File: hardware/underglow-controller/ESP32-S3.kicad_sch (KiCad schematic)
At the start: 47 parts, among them J6 CONSOLE, J7 U.FL-R-SMT-1(10), SW2 SW_Push, SW3 SW_Push, U4 ESP32-S3R2, U5 W25Q128JVS, Y2 40MHZ, Y3 32.7k

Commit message: i can't believe what they did to my boy
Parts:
- removed C19, C23: 10pF, Capacitor_SMD:C_0402_1005Metric, symbol Device:C_Small
- removed TP10: CS1, TestPoint:TestPoint_Pad_D1.0mm, symbol Connector:TestPoint
- removed TP11: CS2, TestPoint:TestPoint_Pad_D1.0mm, symbol Connector:TestPoint
- removed TP2: CHIP_PU, TestPoint:TestPoint_Pad_D1.0mm, symbol Connector:TestPoint
- removed TP5: MOSI, TestPoint:TestPoint_Pad_D1.0mm, symbol Connector:TestPoint
- removed TP6: MISO, TestPoint:TestPoint_Pad_D1.0mm, symbol Connector:TestPoint
- removed TP8: SCLK, TestPoint:TestPoint_Pad_D1.0mm, symbol Connector:TestPoint
- removed TP9: CS0, TestPoint:TestPoint_Pad_D1.0mm, symbol Connector:TestPoint
- removed Y3: 32.7k, Crystal:Crystal_SMD_MicroCrystal_CC7V-T1A-2Pin_3.2x1.5mm, symbol Device:Crystal_Small
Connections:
- net CAN_N: now also U4.24 (GPIO18); no longer U4.23 (GPIO17)
- net CAN_P: now also U4.23 (GPIO17); no longer U4.24 (GPIO18)
- net FSPICS1: now also U4.5 (GPIO0); no longer U4.14 (GPIO9)
- net FSPICS2: now also U4.38 (GPIO33); no longer U4.18 (GPIO13)
- net SX1276_IRQ: now also U4.7 (GPIO2); no longer U4.6 (GPIO1)
- net SX1276_RESET: now also U4.6 (GPIO1); no longer U4.7 (GPIO2)
- net VSENSE: now also U4.18 (GPIO13); no longer U4.43 (GPIO38)
- no-connect marks 8 -> 7
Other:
- note removed: "CX1 = CX2 = 2(7pF - 2pF) = 10pF"

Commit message: updates nearly complete
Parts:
- C10, C14, C4, C7, C8: MPN C0805C104M3RAC7800 -> 560L104YTT
- C12, C15, C16: MPN (none) -> GRT21BC81A106KE01L
- R16, R17, R22, R28: MPN (none) -> RC0402JR-070RP
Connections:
- net SPICS1 is gone; now on net MCPWM_FAULT: U4.28 (SPICS1)
- net GPIO45: now also U4.51 (GPIO45)
- net GPIO46: now also U4.52 (GPIO46)
- no-connect marks 7 -> 5
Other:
- moved on the sheet: C18, C22, Y2

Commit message: add USB VIN
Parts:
- renumbered AE2 to AE4, C10 to C38, C11 to C39, C12 to C40, C14 to C41, C16 to C42, C13 to C43, C15 to C44, C8 to C45, C7 to C46, C17 to C47, C20 to C48, C21 to C49, C4 to C50, C37 to C51, C18 to C52, C22 to C53, J6 to J4, J7 to J5, L3 to L10, L4 to L11, R4 to R13, R6 to R14, R16 to R15, R17 to R16, R22 to R17, R15 to R18, R28 to R19, R25 to R20, R26 to R21, R27 to R22, SW2 to SW4, SW3 to SW5, U4 to U5, U5 to U6, Y2 to Y4

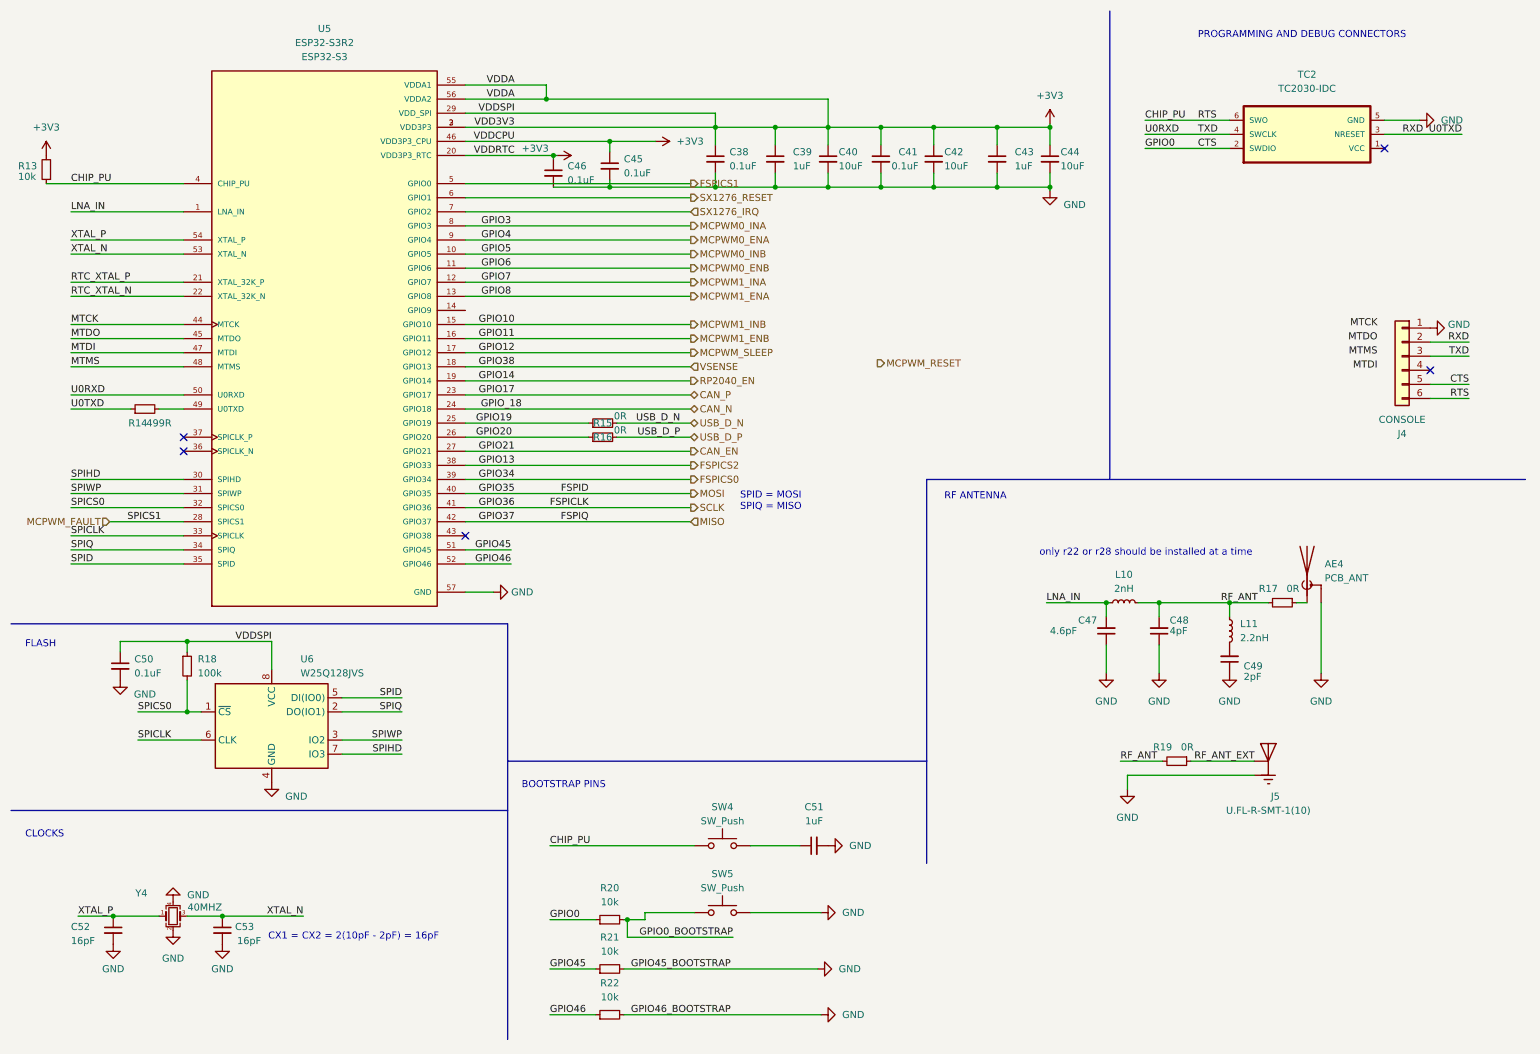
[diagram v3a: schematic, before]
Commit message: Hardware updates
* fix messed up +12v pin
* add a ground output for neopixels on both channels
* add a i2c microphone
* clean up schematic
* calculate component values for the LED drivers
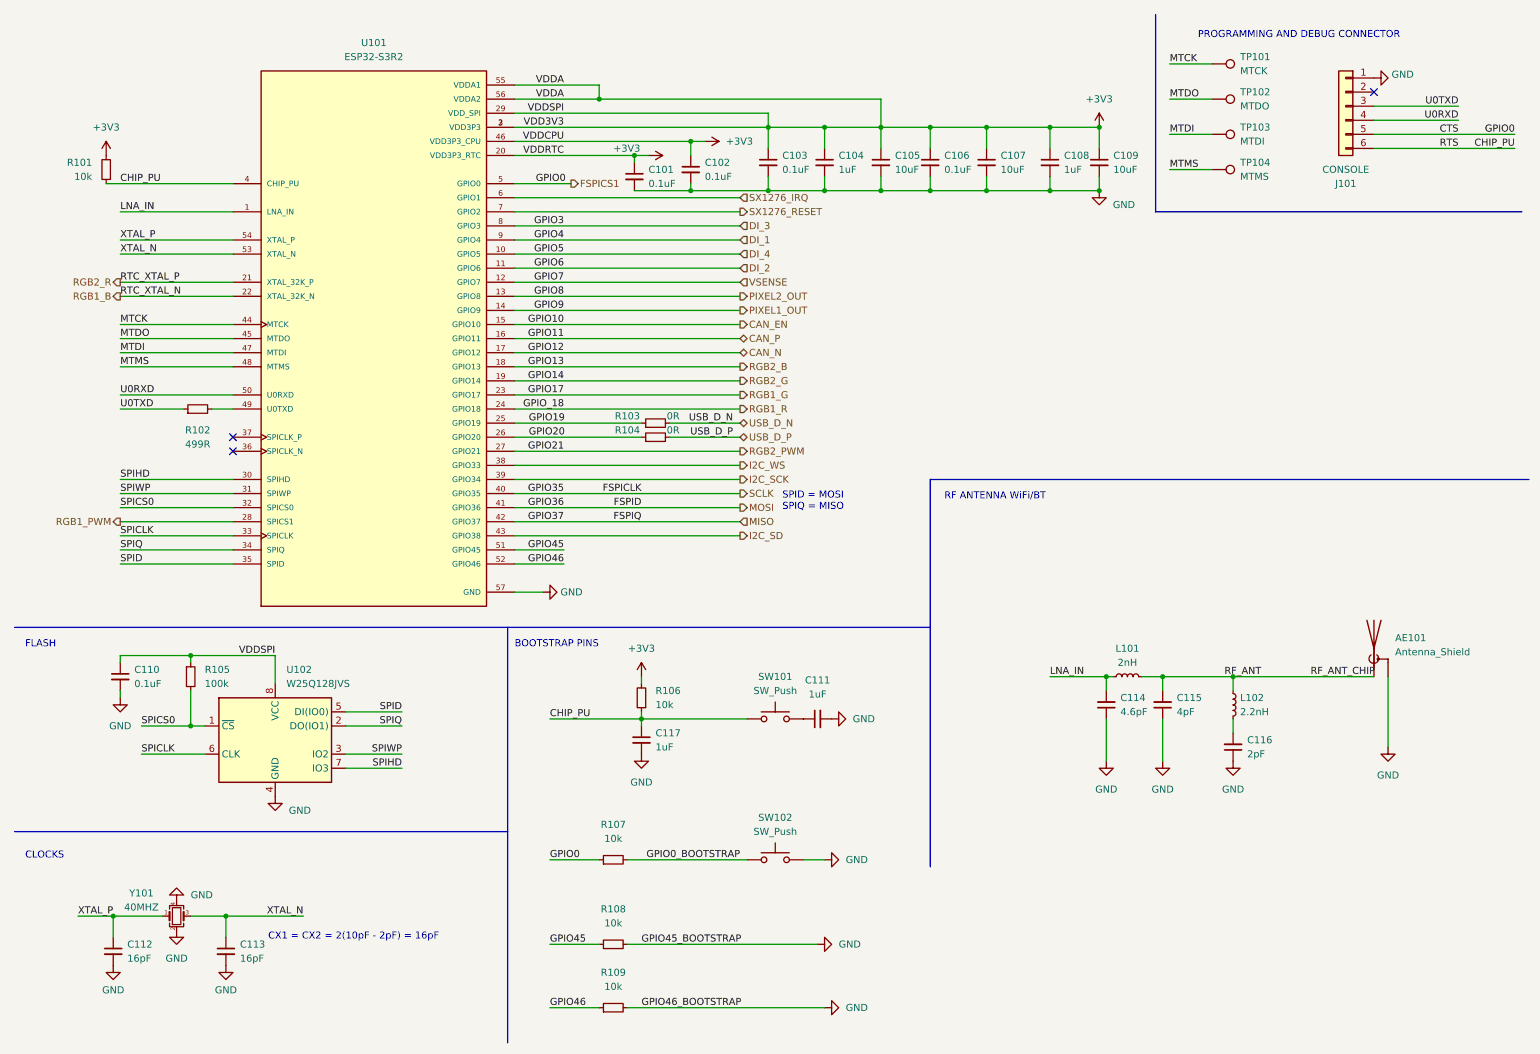
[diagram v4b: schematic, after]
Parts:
- removed AE4: PCB_ANT, RF_Antenna:Texas_SWRA117D_2.4GHz_Right, symbol Device:Antenna_Shield
- removed J5: U.FL-R-SMT-1(10), ConeCodes:HRS_U.FL-R-SMT-1(10), symbol U.FL-R-SMT-1_10_:U.FL-R-SMT-1(10)
- removed R17, R19: 0R, Resistor_SMD:R_0402_1005Metric, symbol Device:R_Small
- removed TC2: TC2030-IDC, Connector:Tag-Connect_TC2030-IDC-NL_2x03_P1.27mm_Vertical, symbol TDC-2030-IDC:TC2030-IDC
- added AE101: Antenna_Shield, RF_Antenna:Texas_SWRA117D_2.4GHz_Left, symbol Device:Antenna_Shield
- added C117: 1uF, Capacitor_SMD:C_0402_1005Metric, symbol Device:C_Small
- added R106: 10k, Resistor_SMD:R_0402_1005Metric, symbol Device:R_Small
- added TP101: MTCK, TestPoint:TestPoint_Pad_D1.0mm, symbol Connector:TestPoint
- added TP102: MTDO, TestPoint:TestPoint_Pad_D1.0mm, symbol Connector:TestPoint
- added TP103: MTDI, TestPoint:TestPoint_Pad_D1.0mm, symbol Connector:TestPoint
- added TP104: MTMS, TestPoint:TestPoint_Pad_D1.0mm, symbol Connector:TestPoint
- renumbered C46 to C101, C45 to C102, C38 to C103, C39 to C104, C40 to C105, C41 to C106, C42 to C107, C43 to C108, C44 to C109, C50 to C110, C51 to C111, C52 to C112, C53 to C113, C47 to C114, C48 to C115, C49 to C116, J4 to J101, L10 to L101, L11 to L102, R13 to R101, R14 to R102, R15 to R103, R16 to R104, R18 to R105, R20 to R107, R21 to R108, R22 to R109, SW4 to SW101, SW5 to SW102, U5 to U101, U6 to U102, Y4 to Y101
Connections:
- net CTS is gone; now on net FSPICS1: J101.5 (Pin_5), R107.1
- net MCPWM1_ENB is gone; now on net CAN_P: U101.16 (GPIO11)
- net MCPWM1_INA is gone; now on net VSENSE: U101.12 (GPIO7)
- net MCPWM1_INB is gone; now on net CAN_EN: U101.15 (GPIO10)
- net MCPWM_SLEEP is gone; now on net CAN_N: U101.17 (GPIO12)
- net +3V3: now also R106.2
- net CAN_EN: no longer U101.27 (GPIO21)
- net CAN_N: no longer U101.24 (GPIO18)
- net CAN_P: no longer U101.23 (GPIO17)
- net CHIP_PU: now also C117.1, R106.1
- net GND: now also AE101.2 (Shield), C117.2
- net MOSI: now also U101.41 (GPIO36); no longer U101.40 (GPIO35)
- net MTCK: now also TP101.1
- net MTDI: now also TP103.1
- net MTDO: now also TP102.1
- net MTMS: now also TP104.1
- net RF_ANT: now also AE101.1 (A)
- net SCLK: now also U101.40 (GPIO35); no longer U101.41 (GPIO36)
- net SX1276_IRQ: now also U101.6 (GPIO1); no longer U101.7 (GPIO2)
- net SX1276_RESET: now also U101.7 (GPIO2); no longer U101.6 (GPIO1)
- net VSENSE: no longer U101.18 (GPIO13)
- net U0RXD: now reaches J101.4 (Pin_4)
- net U0RXD: now also U101.50 (U0RXD)
- net PIXEL1_OUT: now reaches U101.14 (GPIO9)
- net I2C_SD: now reaches U101.43 (GPIO38)
- net FSPICS0 renamed I2C_SCK
- net FSPICS2 renamed I2C_WS
- net MCPWM0_ENA renamed DI_1
- net MCPWM0_ENB renamed DI_2
- net MCPWM0_INA renamed DI_3
- net MCPWM0_INB renamed DI_4
- net MCPWM1_ENA renamed PIXEL2_OUT
- net MCPWM_FAULT renamed RGB1_PWM
- net RP2040_EN renamed RGB2_G
- net RTC_XTAL_N renamed RGB1_B
- net RTC_XTAL_P renamed RGB2_R
- net RXD: no longer names the net of J101.2 (Pin_2)
- net RXD: no longer R102.1
- net TXD renamed U0TXD
- net U0TXD: now also R102.1; no longer U101.50 (U0RXD)
- new net RGB1_G: U101.23 (GPIO17)
- new net RGB1_R: U101.24 (GPIO18)
- new net RGB2_B: U101.18 (GPIO13)
- new net RGB2_PWM: U101.27 (GPIO21)
- no-connect marks 5 -> 3
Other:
- note added: "PROGRAMMING AND DEBUG CONNECTOR"
- note added: "RF ANTENNA WiFi/BT"
- note removed: "PROGRAMMING AND DEBUG CONNECTORS"
- note removed: "RF ANTENNA"
- note removed: "only r22 or r28 should be installed at a time"
- title: CAN RGB Controller -> CAN RGB Controller V5
- moved on the sheet: C101, C102, C103, C104, C105, C106, C107, C108, C109, C110, C111, C112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

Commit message: Bom fillout + wiring
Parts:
- C117: MPN (none) -> CGA2B1X7T0G105M050BC
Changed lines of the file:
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@@
       (effects (font (size 1.27 1.27)) hide)
     )
-    (property "Description" "" (id 4) (at 125.73 143.51 0)
+    (property "Description" "CAP CER 1UF 4V X7T 0402" (id 4) (at 125.73 143.51 0)
       (effects (font (size 1.27 1.27)) hide)
     )
-    (property "MPN" "" (id 5) (at 125.73 143.51 0)
+    (property "MPN" "CGA2B1X7T0G105M050BC" (id 5) (at 125.73 143.51 0)
       (effects (font (size 1.27 1.27)) hide)
     )

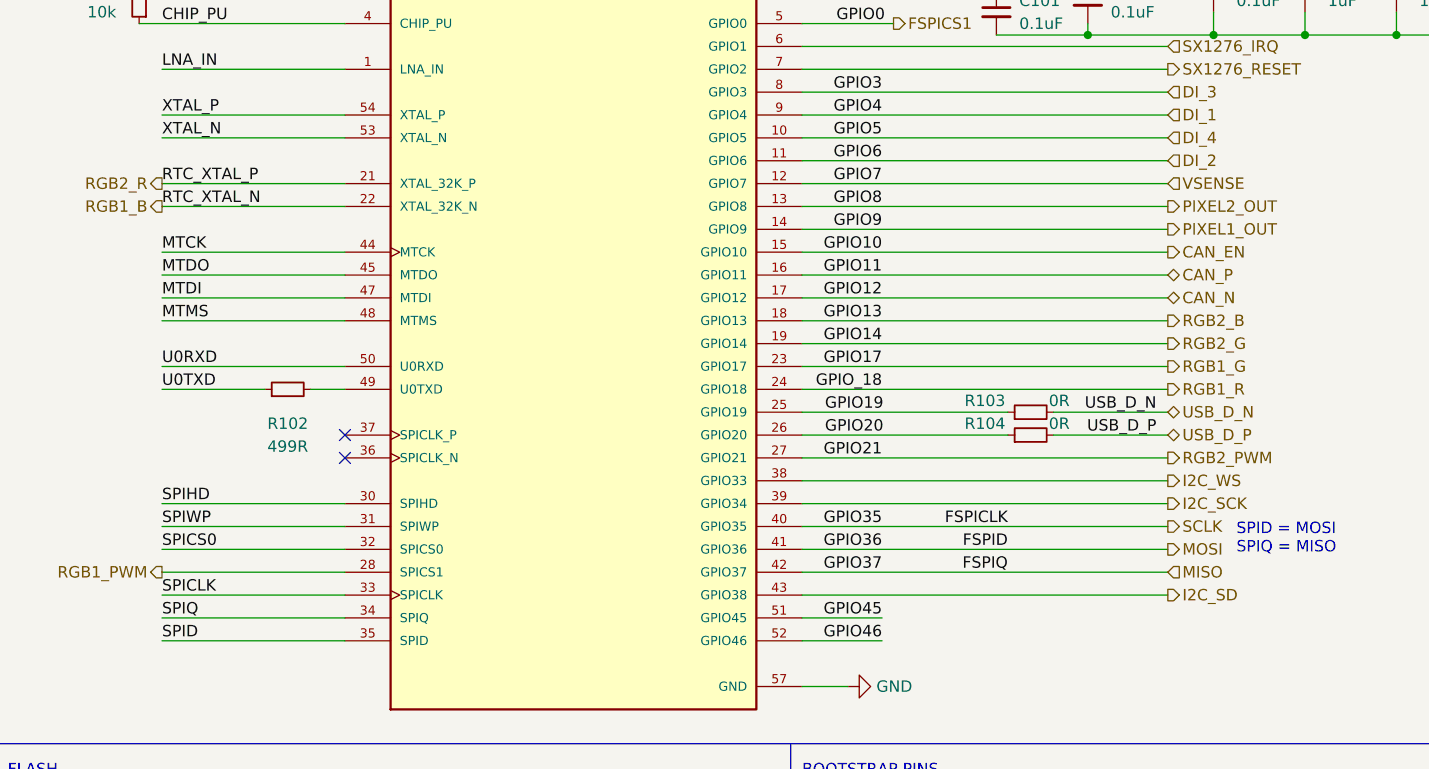
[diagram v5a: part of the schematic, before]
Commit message: hw updates based on prototype issues
* Removes unused hardware and firmware projectes
* Adds some documentation and bom
* cleanup READMEs
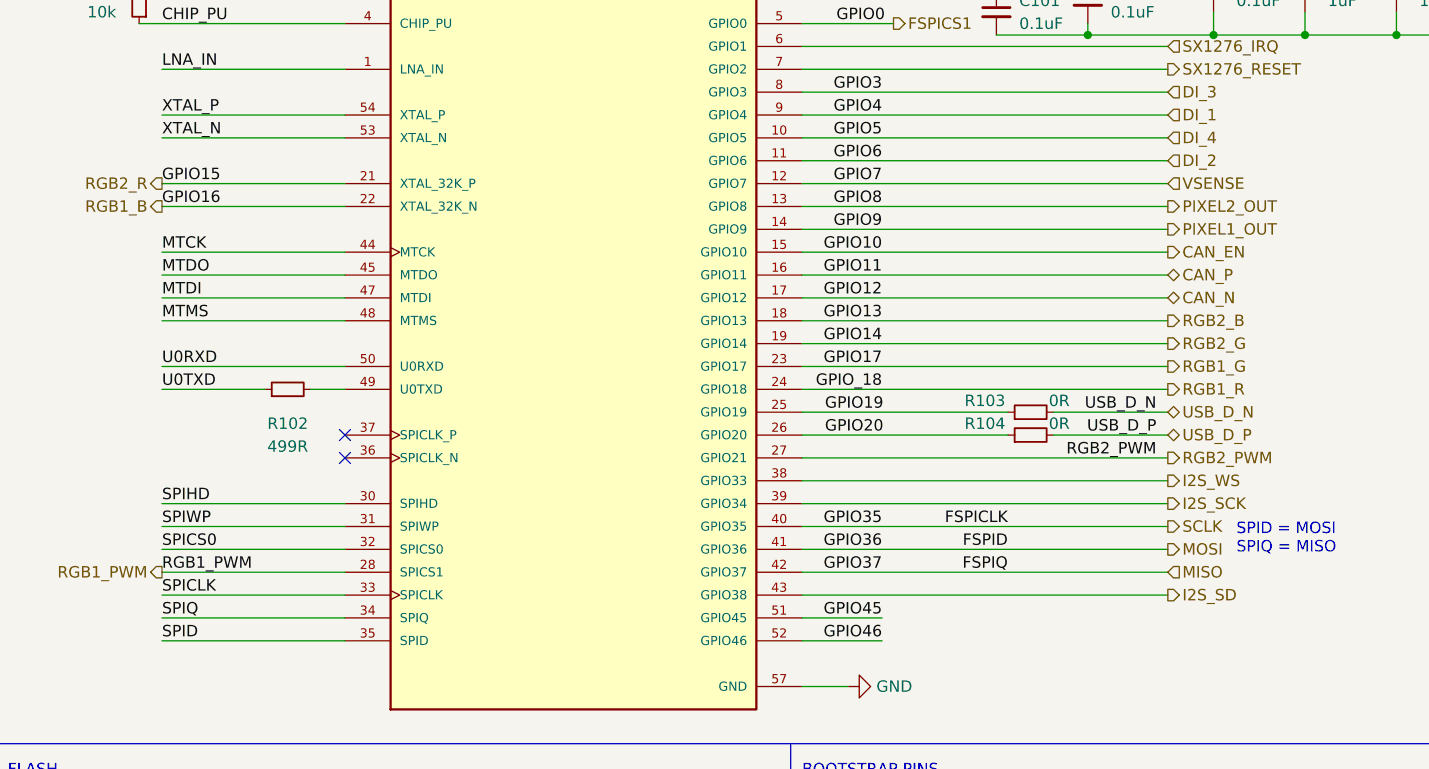
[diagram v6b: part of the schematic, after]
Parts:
- C101, C102, C103, C106, C110: MPN 560L104YTT -> CGA2B1X7R1C104M050BC
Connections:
- net I2C_SCK renamed I2S_SCK
- net I2C_SD renamed I2S_SD
- net I2C_WS renamed I2S_WS
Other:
- company: cone.codes -> Connor Rigby
- title: CAN RGB Controller V5 -> ${Title}
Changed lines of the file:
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@@
   (paper "A4")
   (title_block
-    (title "CAN RGB Controller V5")
+    (title "${Title}")
     (date "2022-06-24")
-    (rev "A")
-    (company "cone.codes")
+    (rev "${Revision}")
+    (company "Connor Rigby")
     (comment 1 "https://github.com/miata-bot/can-link")
+    (comment 2 "https://cone.codes")
   )
   (junction (at 199.39 33.02) (diameter 0) (color 0 0 0 0)
@@
     (effects (font (size 1.27 1.27)) (justify left bottom))
   )
+  (label "RGB2_PWM" (at 142.24 91.44 180)
+    (effects (font (size 1.27 1.27)) (justify right bottom))
+  )
   (label "LNA_IN" (at 31.75 48.26 0)
     (effects (font (size 1.27 1.27)) (justify left bottom))
@@
     (effects (font (size 1.27 1.27)) (justify right bottom))
   )
+  (label "RGB1_PWM" (at 31.75 104.14 0)
+    (effects (font (size 1.27 1.27)) (justify left bottom))
+  )
   (label "GPIO20" (at 105.41 88.9 0)
     (effects (font (size 1.27 1.27)) (justify left bottom))
@@
     (effects (font (size 1.27 1.27)) (justify left bottom))
   )
-  (label "RTC_XTAL_N" (at 31.75 63.5 0)
+  (label "GPIO16" (at 31.75 63.5 0)
     (effects (font (size 1.27 1.27)) (justify left bottom))
   )
@@
     (effects (font (size 1.27 1.27)) (justify left bottom))
   )
-  (label "RTC_XTAL_P" (at 31.75 60.96 0)
+  (label "GPIO15" (at 31.75 60.96 0)
     (effects (font (size 1.27 1.27)) (justify left bottom))
   )
@@
     (effects (font (size 1.27 1.27)) (justify right bottom))
   )
-  (label "GPIO21" (at 111.76 91.44 180)
-    (effects (font (size 1.27 1.27)) (justify right bottom))
-  )
   (label "GPIO3" (at 111.76 50.8 180)
     (effects (font (size 1.27 1.27)) (justify right bottom))
@@
     (effects (font (size 1.27 1.27)) (justify left))
   )
-  (hierarchical_label "I2C_WS" (shape output) (at 143.51 93.98 0)
+  (hierarchical_label "I2S_WS" (shape output) (at 143.51 93.98 0)
     (effects (font (size 1.27 1.27)) (justify left))
   )
@@
     (effects (font (size 1.27 1.27)) (justify right))
   )
-  (hierarchical_label "I2C_SCK" (shape output) (at 143.51 96.52 0)
+  (hierarchical_label "I2S_SCK" (shape output) (at 143.51 96.52 0)
     (effects (font (size 1.27 1.27)) (justify left))
   )
@@
     (effects (font (size 1.27 1.27)) (justify left))
   )
-  (hierarchical_label "I2C_SD" (shape output) (at 143.51 106.68 0)
+  (hierarchical_label "I2S_SD" (shape output) (at 143.51 106.68 0)
     (effects (font (size 1.27 1.27)) (justify left))
   )
@@
       (effects (font (size 1.27 1.27)) hide)
     )
-    (property "MPN" "560L104YTT" (id 5) (at 134.62 40.64 0)
+    (property "MPN" "CGA2B1X7R1C104M050BC" (id 5) (at 134.62 40.64 0)
       (effects (font (size 1.27 1.27)) hide)
     )
@@
       (effects (font (size 1.27 1.27)) hide)
     )
-    (property "MPN" "560L104YTT" (id 5) (at 31.75 132.08 0)
+    (property "MPN" "CGA2B1X7R1C104M050BC" (id 5) (at 31.75 132.08 0)
       (effects (font (size 1.27 1.27)) hide)
     )
@@
       (effects (font (size 1.27 1.27)) hide)
     )
-    (property "MPN" "560L104YTT" (id 5) (at 124.46 41.91 0)
+    (property "MPN" "CGA2B1X7R1C104M050BC" (id 5) (at 124.46 41.91 0)
       (effects (font (size 1.27 1.27)) hide)
     )
@@
       (effects (font (size 1.27 1.27)) hide)
     )
-    (property "MPN" "560L104YTT" (id 5) (at 148.59 39.37 0)
+    (property "MPN" "CGA2B1X7R1C104M050BC" (id 5) (at 148.59 39.37 0)
       (effects (font (size 1.27 1.27)) hide)
     )
@@
       (effects (font (size 1.27 1.27)) hide)
     )
-    (property "MPN" "560L104YTT" (id 5) (at 177.8 39.37 0)
-      (effects (font (size 1.27 1.27)) hide)
-    )
+    (property "MPN" "CGA2B1X7R1C104M050BC" (id 5) (at 177.8 39.37 0)
+      (effects (font (size 1.27 1.27)) hide)
+    )

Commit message: V5 Rev B Hardware release
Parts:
- TP101, TP102, TP103, TP104: now left out of the parts list
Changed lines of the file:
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@@
   )
   (symbol (lib_id "Connector:TestPoint") (at 228.6 21.59 270) (unit 1)
-    (in_bom yes) (on_board yes) (fields_autoplaced)
+    (in_bom no) (on_board yes) (fields_autoplaced)
     (property "Reference" "TP101" (id 0) (at 233.68 20.3199 90)
       (effects (font (size 1.27 1.27)) (justify left))
@@
   )
   (symbol (lib_id "Connector:TestPoint") (at 228.6 34.29 270) (unit 1)
-    (in_bom yes) (on_board yes) (fields_autoplaced)
+    (in_bom no) (on_board yes) (fields_autoplaced)
     (property "Reference" "TP103" (id 0) (at 233.68 33.0199 90)
       (effects (font (size 1.27 1.27)) (justify left))
@@
   )
   (symbol (lib_id "Connector:TestPoint") (at 228.6 40.64 270) (unit 1)
-    (in_bom yes) (on_board yes) (fields_autoplaced)
+    (in_bom no) (on_board yes) (fields_autoplaced)
     (property "Reference" "TP104" (id 0) (at 233.68 39.3699 90)
       (effects (font (size 1.27 1.27)) (justify left))
@@
   )
   (symbol (lib_id "Connector:TestPoint") (at 228.6 27.94 270) (unit 1)
-    (in_bom yes) (on_board yes) (fields_autoplaced)
+    (in_bom no) (on_board yes) (fields_autoplaced)
     (property "Reference" "TP102" (id 0) (at 233.68 26.6699 90)
       (effects (font (size 1.27 1.27)) (justify left))
